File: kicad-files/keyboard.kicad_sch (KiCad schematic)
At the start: 187 parts, among them J1 TYPE-C-31-M12_13, Q1 2N7002, Q2 2N7002, SW1 K2-1187SQ-A4SW-06, T1 53261-0471, T2 53261-0471, U1 STM32F411CEU6, U2 USBLC6-2SC6, U3 AT24C256C-SSHL-T, U4 SGM2007-3.3XN5/TR, Y1 TAXM8M4RFDCET2T

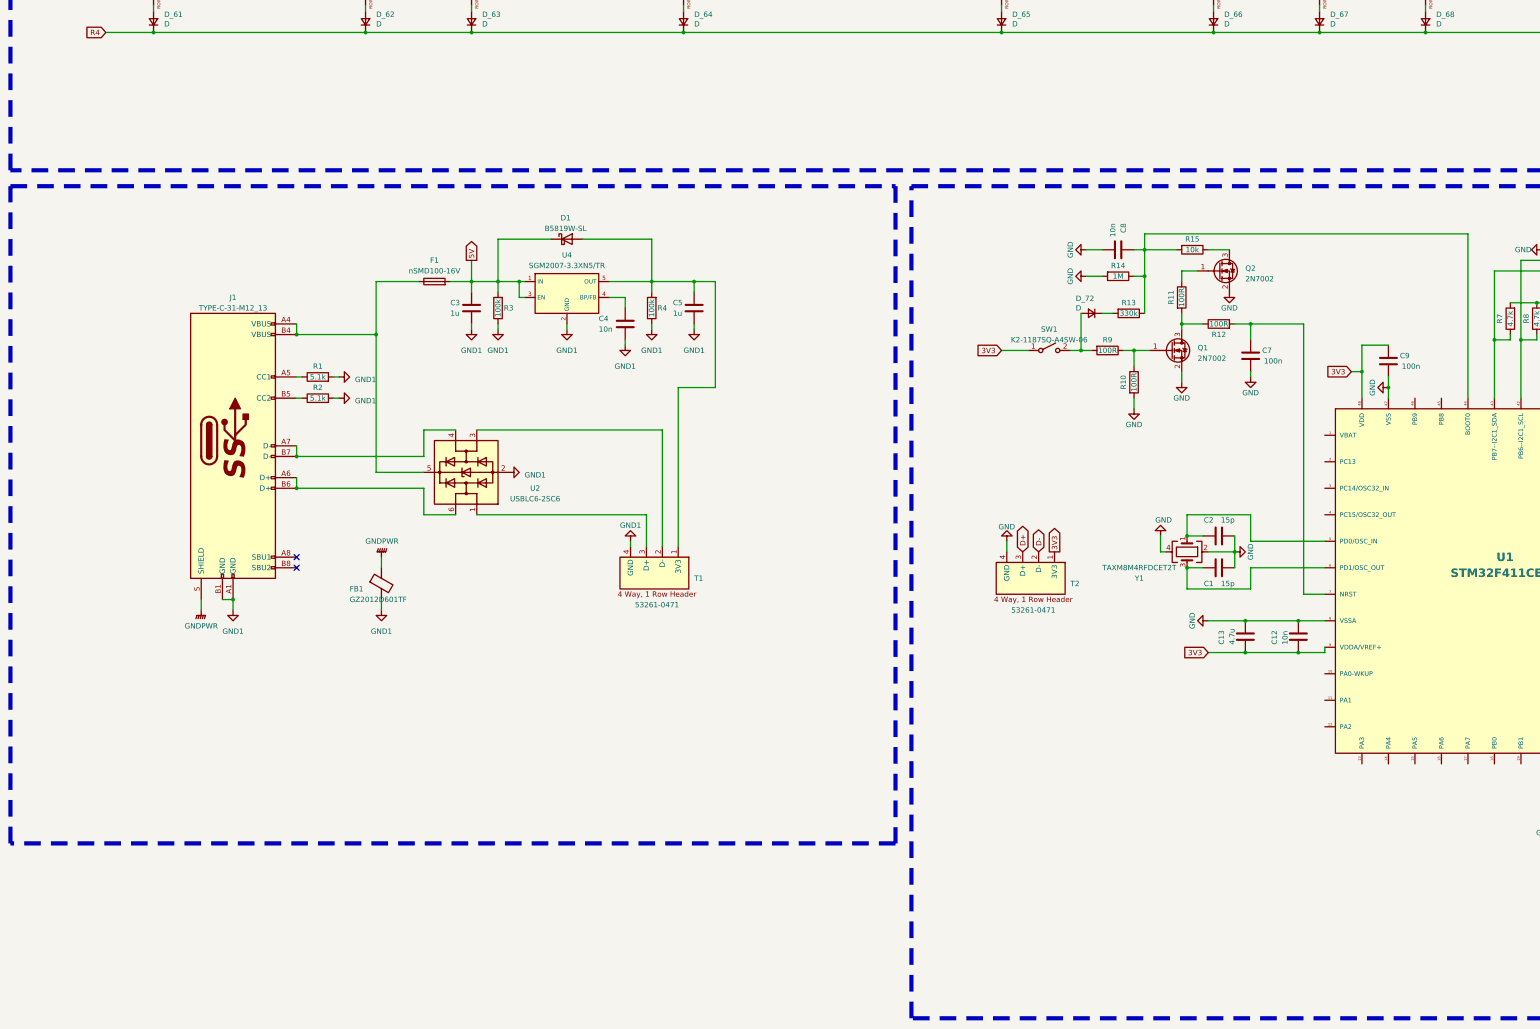
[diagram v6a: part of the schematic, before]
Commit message: Connected all 3V3 to STM
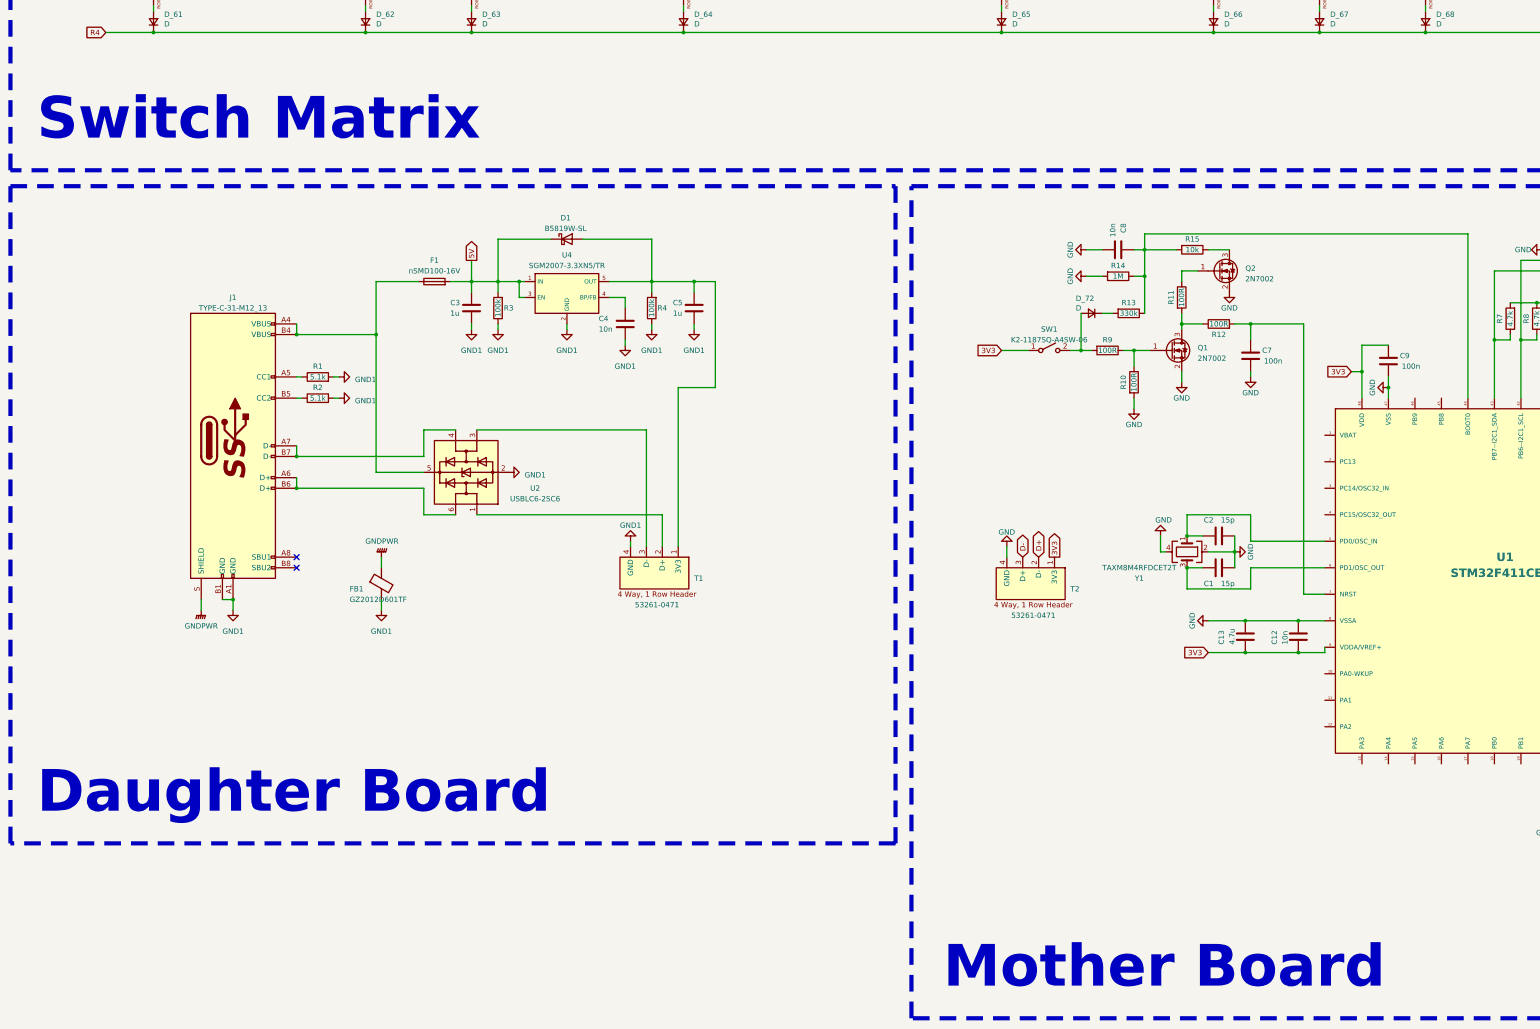
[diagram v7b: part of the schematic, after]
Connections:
- net D+: now also T2.2 (D-); no longer T2.3 (D+)
- net D-: now also T2.3 (D+); no longer T2.2 (D-)
- net at T1.2 (D+): now also U2.1 (I/O1); no longer U2.3 (I/O2)
- net at T1.3 (D-): now also U2.3 (I/O2); no longer U2.1 (I/O1)
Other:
- note added: "Daughter Board"
- note added: "Mother Board"
- note added: "Switch Matrix"
- moved on the sheet: T2
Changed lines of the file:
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@@
     (stroke (width 0) (type default))
   )
+  (wire (pts (xy 345.44 370.84) (xy 300.99 370.84))
+    (stroke (width 0) (type default))
+  )
   (wire (pts (xy 361.95 193.04) (xy 361.95 167.64))
     (stroke (width 0) (type default))
@@
     (stroke (width 0) (type default))
   )
+  (wire (pts (xy 341.63 350.52) (xy 341.63 378.46))
+    (stroke (width 0) (type default))
+  )
   (wire (pts (xy 431.8 193.04) (xy 438.15 193.04))
     (stroke (width 0) (type default))
@@
     (stroke (width 0) (type default))
   )
+  (wire (pts (xy 300.99 350.52) (xy 341.63 350.52))
+    (stroke (width 0) (type default))
+  )
   (wire (pts (xy 477.52 229.87) (xy 502.92 229.87))
     (stroke (width 0) (type default))
@@
     (stroke (width 0) (type default))
   )
-  (wire (pts (xy 427.99 377.19) (xy 427.99 379.73))
+  (wire (pts (xy 427.99 378.46) (xy 427.99 381))
     (stroke (width 0) (type default))
   )
@@
     (stroke (width 0) (type default))
   )
-  (wire (pts (xy 300.99 370.84) (xy 341.63 370.84))
-    (stroke (width 0) (type default))
-  )
   (wire (pts (xy 482.6 243.84) (xy 488.95 243.84))
     (stroke (width 0) (type default))
@@
     (stroke (width 0) (type default))
   )
-  (wire (pts (xy 300.99 350.52) (xy 345.44 350.52))
-    (stroke (width 0) (type default))
-  )
   (wire (pts (xy 223.52 153.67) (xy 248.92 153.67))
     (stroke (width 0) (type default))
@@
     (stroke (width 0) (type default))
   )
-  (wire (pts (xy 341.63 370.84) (xy 341.63 378.46))
-    (stroke (width 0) (type default))
-  )
   (wire (pts (xy 577.85 312.42) (xy 577.85 309.88))
     (stroke (width 0) (type default))
@@
     (stroke (width 0) (type default))
   )
+  (wire (pts (xy 345.44 378.46) (xy 345.44 370.84))
+    (stroke (width 0) (type default))
+  )
   (wire (pts (xy 248.92 147.32) (xy 248.92 148.59))
     (stroke (width 0) (type default))
@@
     (stroke (width 0) (type default))
   )
-  (wire (pts (xy 345.44 350.52) (xy 345.44 378.46))
-    (stroke (width 0) (type default))
-  )
   (wire (pts (xy 452.12 229.87) (xy 477.52 229.87))
     (stroke (width 0) (type default))
@@
     (fill (type none))
   )
+  (text "Switch Matrix" (at 195.58 281.94 0)
+    (effects (font (size 10 10) (thickness 2) bold (color 72 72 72 1)) (justify left bottom))
+  )
+  (text "Mother Board" (at 412.75 485.14 0)
+    (effects (font (size 10 10) (thickness 2) bold (color 72 72 72 1)) (justify left bottom))
+  )
+  (text "Daughter Board" (at 195.58 443.23 0)
+    (effects (font (size 10 10) (thickness 2) bold (color 72 72 72 1)) (justify left bottom))
+  )
   (global_label "D+" (shape bidirectional) (at 609.6 372.11 0) (fields_autoplaced)
     (effects (font (size 1.27 1.27)) (justify left))
@@
     )
   )
-  (global_label "3V3" (shape output) (at 439.42 379.73 90) (fields_autoplaced)
+  (global_label "3V3" (shape output) (at 439.42 381 90) (fields_autoplaced)
     (effects (font (size 1.27 1.27)) (justify left))
-    (property "Intersheetrefs" "${INTERSHEET_REFS}" (at 439.42 373.9708 90)
+    (property "Intersheetrefs" "${INTERSHEET_REFS}" (at 439.42 375.2408 90)
       (effects (font (size 1.27 1.27)) (justify left) hide)
     )
@@
     )
   )
-  (global_label "D-" (shape bidirectional) (at 435.61 379.73 90) (fields_autoplaced)
+  (global_label "D-" (shape bidirectional) (at 431.8 381 90) (fields_autoplaced)
     (effects (font (size 1.27 1.27)) (justify left))
-    (property "Intersheetrefs" "${INTERSHEET_REFS}" (at 435.61 373.6835 90)
+    (property "Intersheetrefs" "${INTERSHEET_REFS}" (at 431.8 374.9535 90)
       (effects (font (size 1.27 1.27)) (justify left) hide)
     )
@@
     )
   )
-  (global_label "D+" (shape bidirectional) (at 431.8 379.73 90) (fields_autoplaced)
+  (global_label "D+" (shape bidirectional) (at 435.61 381 90) (fields_autoplaced)
     (effects (font (size 1.27 1.27)) (justify left))
-    (property "Intersheetrefs" "${INTERSHEET_REFS}" (at 431.8 373.6835 90)
+    (property "Intersheetrefs" "${INTERSHEET_REFS}" (at 435.61 374.9535 90)
       (effects (font (size 1.27 1.27)) (justify left) hide)
     )
@@
     )
   )
-  (symbol (lib_id "power:GND") (at 427.99 377.19 180) (unit 1)
+  (symbol (lib_id "power:GND") (at 427.99 378.46 180) (unit 1)
     (in_bom yes) (on_board yes) (dnp no)
-    (property "Reference" "#PWR031" (at 427.99 370.84 0)
+    (property "Reference" "#PWR031" (at 427.99 372.11 0)
       (effects (font (size 1.27 1.27)) hide)
     )
-    (property "Value" "GND" (at 425.9754 373.7403 0)
+    (property "Value" "GND" (at 425.9754 375.0103 0)
       (effects (font (size 1.27 1.27)) (justify right))
     )
-    (property "Footprint" "" (at 427.99 377.19 0)
+    (property "Footprint" "" (at 427.99 378.46 0)
       (effects (font (size 1.27 1.27)) hide)
     )
-    (property "Datasheet" "" (at 427.99 377.19 0)
+    (property "Datasheet" "" (at 427.99 378.46 0)
       (effects (font (size 1.27 1.27)) hide)
     )
@@
     )
   )
-  (symbol (lib_id "legshark_symbols:Header_4_Way,_1_Row") (at 344.17 384.81 270) (unit 1)
+  (symbol (lib_name "Header_4_Way,_1_Row_1") (lib_id "legshark_symbols:Header_4_Way,_1_Row") (at 344.17 384.81 270) (unit 1)
     (in_bom yes) (on_board yes) (dnp no)
     (property "Reference" "T1" (at 353.06 386.08 90)
@@
     )
   )
-  (symbol (lib_id "legshark_symbols:Header_4_Way,_1_Row") (at 434.34 386.08 270) (unit 1)
+  (symbol (lib_id "legshark_symbols:Header_4_Way,_1_Row") (at 434.34 387.35 270) (unit 1)
     (in_bom yes) (on_board yes) (dnp no)
-    (property "Reference" "T2" (at 443.23 387.35 90)
+    (property "Reference" "T2" (at 443.23 388.62 90)
       (effects (font (size 1.27 1.27)) (justify left))
     )
-    (property "Value" "53261-0471" (at 434.34 393.7 90)
+    (property "Value" "53261-0471" (at 434.34 394.97 90)
       (effects (font (size 1.27 1.27)))
     )
-    (property "Footprint" "Legshark:Molex, PicoBlade, 53261, 4 Way, 1 Row, Right Angle PCB Header" (at 422.91 384.81 0)
+    (property "Footprint" "Legshark:Molex, PicoBlade, 53261, 4 Way, 1 Row, Right Angle PCB Header" (at 422.91 386.08 0)
       (effects (font (size 1.27 1.27)) hide)
     )
-    (property "Datasheet" "https://docs.rs-online.com/4dcc/0900766b8150e34b.pdf" (at 447.04 387.35 0)
+    (property "Datasheet" "https://docs.rs-online.com/4dcc/0900766b8150e34b.pdf" (at 447.04 388.62 0)
       (effects (font (size 1.27 1.27)) hide)
     )

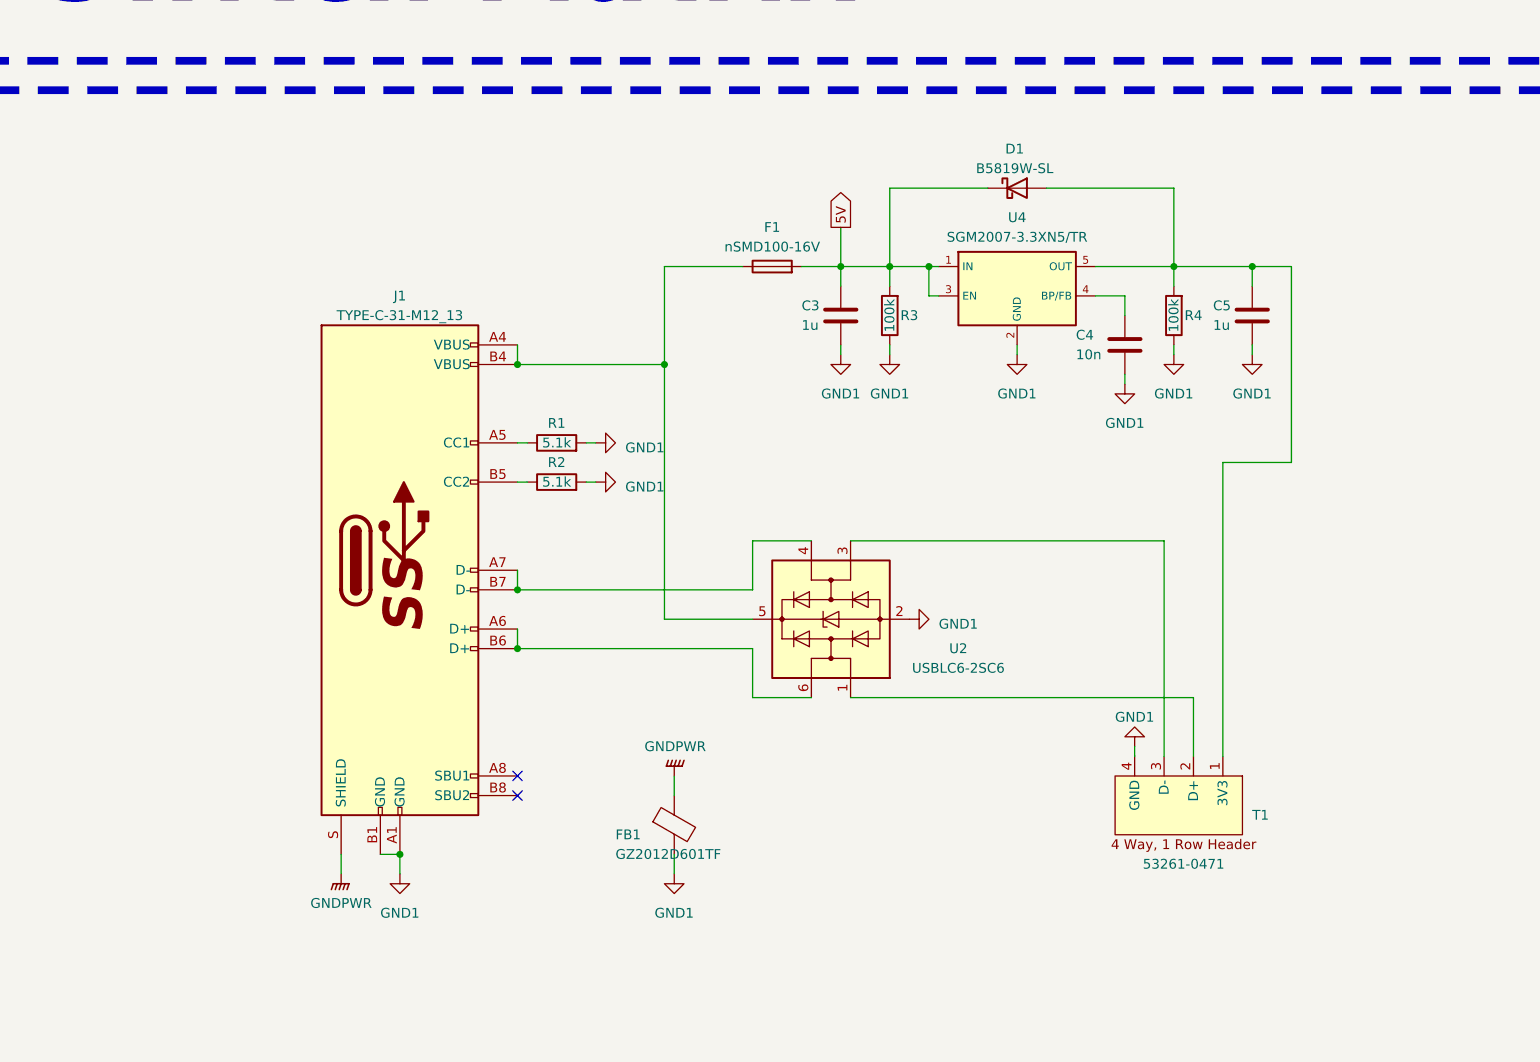
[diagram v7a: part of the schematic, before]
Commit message: Resized MB again & started joining rows
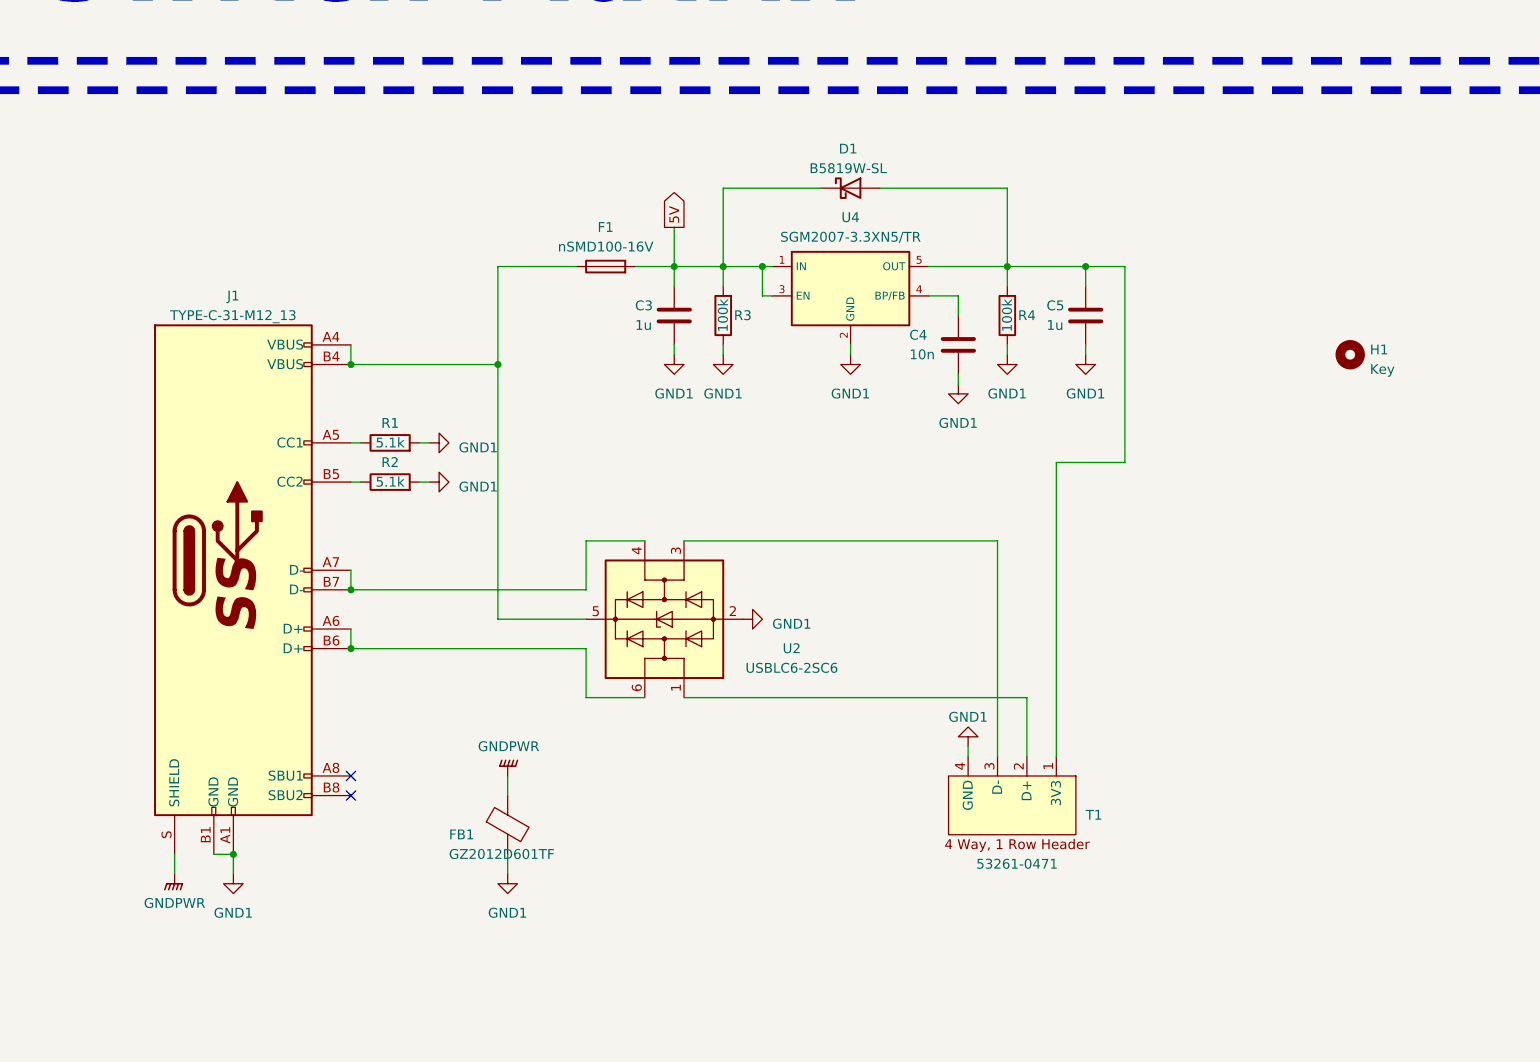
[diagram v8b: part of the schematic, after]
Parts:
- added H1: Key, MountingHole:MountingHole_3.2mm_M3, symbol Mechanical:MountingHole
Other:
- moved on the sheet: C3, C4, C5, D1, F1, FB1, J1, R1, R2, R3, R4, T1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
